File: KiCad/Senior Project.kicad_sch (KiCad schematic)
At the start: 26 parts, among them J1 USB_C_Receptacle_USB2.0_16P, J2 Screw_Terminal_01x02, J3 Screw_Terminal_01x06, SW1 SW_Push, SW2 SW_Push, U1 ESP32-S3FH4R2, X1 FC-135 32.7680KA-A5, Y2 Crystal_GND23

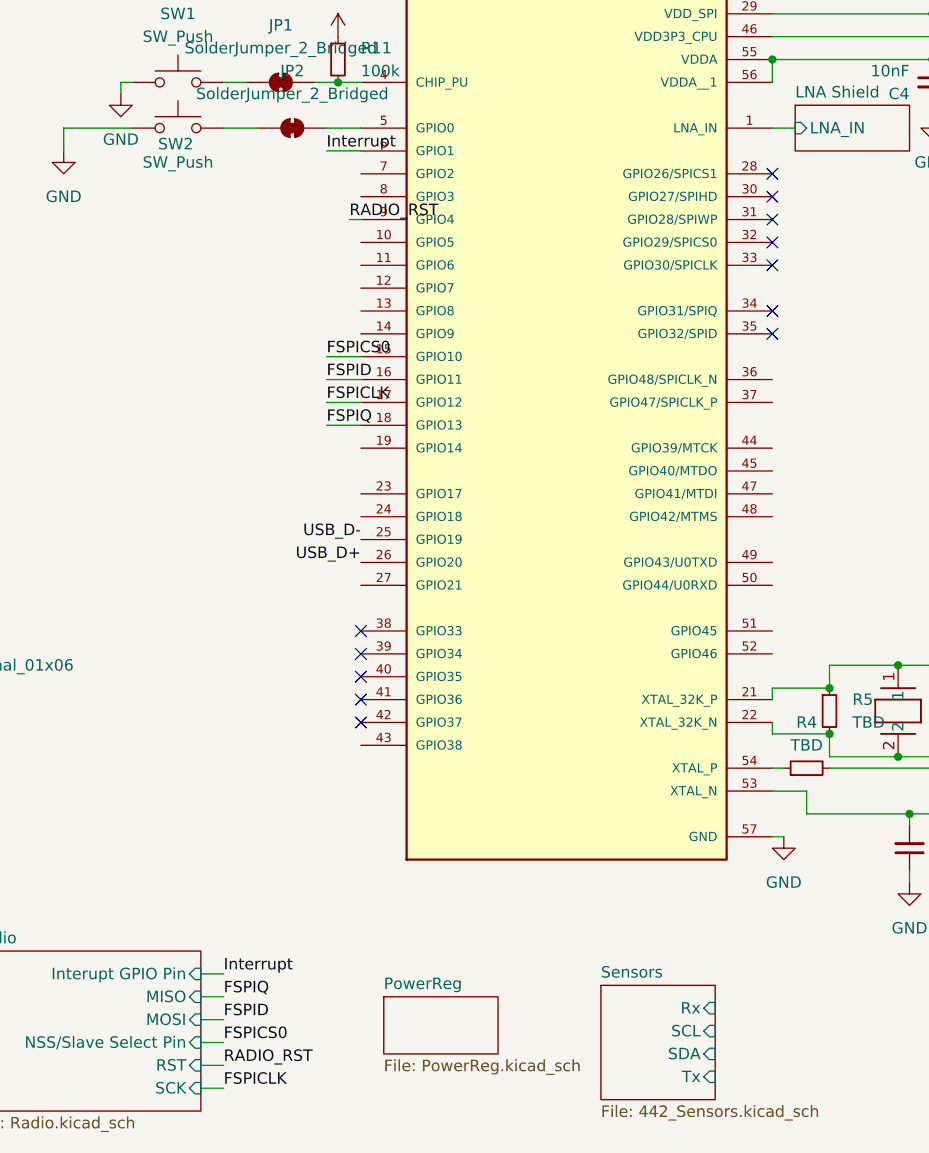
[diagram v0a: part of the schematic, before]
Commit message: I2C connections
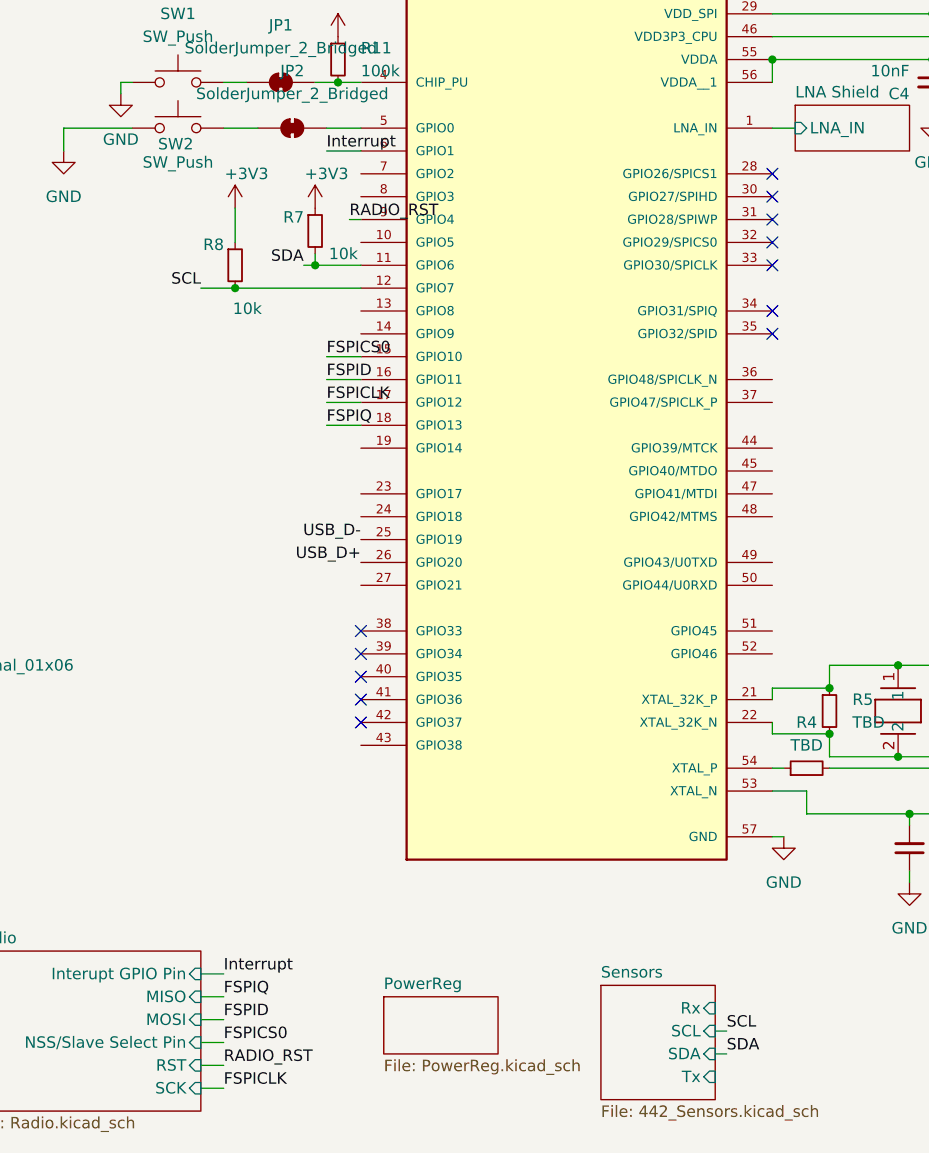
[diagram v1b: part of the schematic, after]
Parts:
- added R7, R8: 10k, Resistor_SMD:R_0402_1005Metric, symbol Device:R_Small
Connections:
- net +3V3: now also R7.1, R8.1
- net SDA: now reaches U1.11 (GPIO6)
- net SDA: now also R7.2
- net SCL: now reaches U1.12 (GPIO7)
- net SCL: now also R8.2

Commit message: Pin adjust
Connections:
- net SCL: now also U1.14 (GPIO9); no longer U1.12 (GPIO7)
- net SDA: now also U1.13 (GPIO8); no longer U1.11 (GPIO6)
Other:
- moved on the sheet: R7, R8
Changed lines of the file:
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@@
 	(paper "A4")
 	(junction
-		(at 106.68 85.09)
+		(at 118.11 62.23)
 		(diameter 0)
 		(color 0 0 0 0)
 	)
 	(junction
-		(at 118.11 62.23)
+		(at 181.61 143.51)
 		(diameter 0)
 		(color 0 0 0 0)
 	)
 	(junction
-		(at 181.61 143.51)
+		(at 105.41 90.17)
 		(diameter 0)
 		(color 0 0 0 0)
@@
 	)
 	(junction
+		(at 114.3 87.63)
+		(diameter 0)
+		(color 0 0 0 0)
+	)
+	(junction
 		(at 170.18 52.07)
 		(diameter 0)
@@
 		(color 0 0 0 0)
 	)
-	(junction
-		(at 115.57 82.55)
-		(diameter 0)
-		(color 0 0 0 0)
-	)
 	(no_connect
 		(at 166.37 74.93)
@@
 	(wire
 		(pts
-			(xy 102.87 85.09) (xy 106.68 85.09)
+			(xy 101.6 90.17) (xy 105.41 90.17)
 		)
 		(stroke
@@
 	(wire
 		(pts
-			(xy 114.3 82.55) (xy 115.57 82.55)
+			(xy 113.03 87.63) (xy 114.3 87.63)
+		)
+		(stroke
+			(width 0)
+			(type default)
+		)
+	)
+	(wire
+		(pts
+			(xy 105.41 90.17) (xy 120.65 90.17)
 		)
 		(stroke
@@
 	(wire
 		(pts
-			(xy 115.57 81.28) (xy 115.57 82.55)
+			(xy 114.3 86.36) (xy 114.3 87.63)
 		)
 		(stroke
@@
 	(wire
 		(pts
-			(xy 106.68 80.01) (xy 106.68 76.2)
+			(xy 105.41 85.09) (xy 105.41 81.28)
 		)
 		(stroke
@@
 	(wire
 		(pts
-			(xy 106.68 85.09) (xy 120.65 85.09)
-		)
-		(stroke
-			(width 0)
-			(type default)
-		)
-	)
-	(wire
-		(pts
 			(xy 64.77 49.53) (xy 69.85 49.53)
 		)
@@
 	(wire
 		(pts
-			(xy 115.57 82.55) (xy 120.65 82.55)
-		)
-		(stroke
-			(width 0)
-			(type default)
-		)
-	)
-	(wire
-		(pts
 			(xy 116.84 67.31) (xy 120.65 67.31)
 		)
@@
 	(wire
 		(pts
+			(xy 114.3 87.63) (xy 120.65 87.63)
+		)
+		(stroke
+			(width 0)
+			(type default)
+		)
+	)
+	(wire
+		(pts
 			(xy 102.87 163.83) (xy 105.41 163.83)
 		)
@@
 	)
 	(label "SDA"
-		(at 114.3 82.55 180)
+		(at 113.03 87.63 180)
 		(effects
 			(font
@@
 	)
 	(label "SCL"
-		(at 102.87 85.09 180)
+		(at 101.6 90.17 180)
 		(effects
 			(font
@@
 	(symbol
 		(lib_id "Device:R_Small")
-		(at 106.68 82.55 0)
+		(at 105.41 87.63 0)
 		(unit 1)
 		(exclude_from_sim no)
@@
 		(dnp no)
 		(property "Reference" "R8"
-			(at 103.124 80.264 0)
+			(at 101.854 85.344 0)
 			(effects
 				(font
@@
 		)
 		(property "Value" "10k"
-			(at 106.426 87.376 0)
+			(at 105.156 92.456 0)
 			(effects
 				(font
@@
 		)
 		(property "Footprint" "Resistor_SMD:R_0402_1005Metric"
-			(at 106.68 82.55 0)
+			(at 105.41 87.63 0)
 			(effects
 				(font
@@
 		)
 		(property "Datasheet" "~"
-			(at 106.68 82.55 0)
+			(at 105.41 87.63 0)
 			(effects
 				(font
@@
 		)
 		(property "Description" "Resistor, small symbol"
-			(at 106.68 82.55 0)
+			(at 105.41 87.63 0)
 			(effects
 				(font
@@
 	(symbol
 		(lib_id "power:+3V3")
-		(at 106.68 76.2 0)
+		(at 105.41 81.28 0)
 		(unit 1)
 		(exclude_from_sim no)
@@
 		(dnp no)
 		(property "Reference" "#PWR076"
-			(at 106.68 80.01 0)
+			(at 105.41 85.09 0)
 			(effects
 				(font
@@
 		)
 		(property "Value" "+3V3"
-			(at 107.95 72.39 0)
+			(at 106.68 77.47 0)
 			(effects
 				(font
@@
 		)
 		(property "Footprint" ""
-			(at 106.68 76.2 0)
+			(at 105.41 81.28 0)
 			(effects
 				(font
@@
 		)
 		(property "Datasheet" ""
-			(at 106.68 76.2 0)
+			(at 105.41 81.28 0)
 			(effects
 				(font
@@
 		)
 		(property "Description" "Power symbol creates a global label with name \"+3V3\""
-			(at 106.68 76.2 0)
+			(at 105.41 81.28 0)
 			(effects
 				(font
@@
 	(symbol
 		(lib_id "Device:R_Small")
-		(at 115.57 78.74 0)
+		(at 114.3 83.82 0)
 		(unit 1)
 		(exclude_from_sim no)
@@
 		(dnp no)
 		(property "Reference" "R7"
-			(at 112.014 77.216 0)
+			(at 110.744 82.296 0)
 			(effects
 				(font
@@
 		)
 		(property "Value" "10k"
-			(at 117.094 81.28 0)
+			(at 115.824 86.36 0)
 			(effects
 				(font
@@
 		)
 		(property "Footprint" "Resistor_SMD:R_0402_1005Metric"
-			(at 115.57 78.74 0)
+			(at 114.3 83.82 0)
 			(effects
 				(font
@@
 		)
 		(property "Datasheet" "~"
-			(at 115.57 78.74 0)
+			(at 114.3 83.82 0)
 			(effects
 				(font
@@
 		)
 		(property "Description" "Resistor, small symbol"
-			(at 115.57 78.74 0)
+			(at 114.3 83.82 0)
 			(effects
 				(font
@@
 	(symbol
 		(lib_id "power:+3V3")
-		(at 115.57 76.2 0)
+		(at 114.3 81.28 0)
 		(unit 1)
 		(exclude_from_sim no)
@@
 		(dnp no)
 		(property "Reference" "#PWR077"
-			(at 115.57 80.01 0)
+			(at 114.3 85.09 0)
 			(effects
 				(font
@@
 		)
 		(property "Value" "+3V3"
-			(at 116.84 72.39 0)
+			(at 115.57 77.47 0)
 			(effects
 				(font
@@
 		)
 		(property "Footprint" ""
-			(at 115.57 76.2 0)
+			(at 114.3 81.28 0)
 			(effects
 				(font
@@
 		)
 		(property "Datasheet" ""
-			(at 115.57 76.2 0)
+			(at 114.3 81.28 0)
 			(effects
 				(font
@@
 		)
 		(property "Description" "Power symbol creates a global label with name \"+3V3\""
-			(at 115.57 76.2 0)
+			(at 114.3 81.28 0)
 			(effects
 				(font

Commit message: Layout updated. Very little left to do.
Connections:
- net Sense 1: now reaches U1.19 (GPIO14)
- net Sense 2: now reaches U1.23 (GPIO17)
- net Sense 3: now reaches U1.24 (GPIO18)
- net Pyro GPIO 2: now reaches U1.36 (GPIO48/SPICLK_N)
- net Pyro GPIO 3: now reaches U1.37 (GPIO47/SPICLK_P)
- net Pyro GPIO 1: now reaches U1.43 (GPIO38)
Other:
- sheet Sensors ports: added GPS_Reset; removed none
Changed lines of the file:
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@@
 	(wire
 		(pts
+			(xy 41.91 137.16) (xy 43.18 137.16)
+		)
+		(stroke
+			(width 0)
+			(type default)
+		)
+	)
+	(wire
+		(pts
+			(xy 119.38 135.89) (xy 120.65 135.89)
+		)
+		(stroke
+			(width 0)
+			(type default)
+		)
+	)
+	(wire
+		(pts
+			(xy 166.37 97.79) (xy 167.64 97.79)
+		)
+		(stroke
+			(width 0)
+			(type default)
+		)
+	)
+	(wire
+		(pts
 			(xy 184.15 54.61) (xy 191.77 54.61)
 		)
@@
 	(wire
 		(pts
+			(xy 41.91 154.94) (xy 43.18 154.94)
+		)
+		(stroke
+			(width 0)
+			(type default)
+		)
+	)
+	(wire
+		(pts
 			(xy 102.87 161.29) (xy 105.41 161.29)
 		)
@@
 	(wire
 		(pts
+			(xy 41.91 139.7) (xy 43.18 139.7)
+		)
+		(stroke
+			(width 0)
+			(type default)
+		)
+	)
+	(wire
+		(pts
 			(xy 207.01 139.7) (xy 207.01 138.43)
 		)
@@
 	(wire
 		(pts
+			(xy 41.91 121.92) (xy 43.18 121.92)
+		)
+		(stroke
+			(width 0)
+			(type default)
+		)
+	)
+	(wire
+		(pts
 			(xy 116.84 95.25) (xy 120.65 95.25)
 		)
@@
 	(wire
 		(pts
+			(xy 41.91 124.46) (xy 43.18 124.46)
+		)
+		(stroke
+			(width 0)
+			(type default)
+		)
+	)
+	(wire
+		(pts
 			(xy 170.18 140.97) (xy 166.37 140.97)
 		)
@@
 	(wire
 		(pts
+			(xy 41.91 152.4) (xy 43.18 152.4)
+		)
+		(stroke
+			(width 0)
+			(type default)
+		)
+	)
+	(wire
+		(pts
 			(xy 170.18 52.07) (xy 172.72 52.07)
 		)
@@
 	(wire
 		(pts
+			(xy 166.37 95.25) (xy 167.64 95.25)
+		)
+		(stroke
+			(width 0)
+			(type default)
+		)
+	)
+	(wire
+		(pts
 			(xy 102.87 171.45) (xy 105.41 171.45)
 		)
@@
 		)
 	)
+	(label "Sense 2"
+		(at 43.18 139.7 0)
+		(effects
+			(font
+				(size 1.27 1.27)
+			)
+			(justify left bottom)
+		)
+	)
 	(label "SCL"
 		(at 161.29 167.64 0)
@@
 		)
 	)
+	(label "Sense 1"
+		(at 43.18 124.46 0)
+		(effects
+			(font
+				(size 1.27 1.27)
+			)
+			(justify left bottom)
+		)
+	)
 	(label "Interrupt"
 		(at 105.41 161.29 0)
@@
 		)
 	)
+	(label "Pyro GPIO 2"
+		(at 167.64 95.25 0)
+		(effects
+			(font
+				(size 1.27 1.27)
+			)
+			(justify left bottom)
+		)
+	)
 	(label "RADIO_RST"
 		(at 105.41 171.45 0)
@@
 		)
 	)
+	(label "Pyro GPIO 1"
+		(at 43.18 121.92 0)
+		(effects
+			(font
+				(size 1.27 1.27)
+			)
+			(justify left bottom)
+		)
+	)
+	(label "Pyro GPIO 1"
+		(at 119.38 135.89 180)
+		(effects
+			(font
+				(size 1.27 1.27)
+			)
+			(justify right bottom)
+		)
+	)
 	(label "FSPICLK"
 		(at 116.84 97.79 0)
@@
 		)
 	)
+	(label "Pyro GPIO 3"
+		(at 167.64 97.79 0)
+		(effects
+			(font
+				(size 1.27 1.27)
+			)
+			(justify left bottom)
+		)
+	)
 	(label "FSPICS0"
 		(at 116.84 92.71 0)
@@
 		)
 	)
+	(label "Sense 2"
+		(at 120.65 107.95 180)
+		(effects
+			(font
+				(size 1.27 1.27)
+			)
+			(justify right bottom)
+		)
+	)
 	(label "Interrupt"
 		(at 116.84 69.85 0)
@@
 		)
 	)
+	(label "Sense 1"
+		(at 120.65 102.87 180)
+		(effects
+			(font
+				(size 1.27 1.27)
+			)
+			(justify right bottom)
+		)
+	)
+	(label "Pyro GPIO 2"
+		(at 43.18 137.16 0)
+		(effects
+			(font
+				(size 1.27 1.27)
+			)
+			(justify left bottom)
+		)
+	)
 	(label "SDA"
 		(at 161.29 170.18 0)
@@
 		)
 	)
+	(label "Pyro GPIO 3"
+		(at 43.18 152.4 0)
+		(effects
+			(font
+				(size 1.27 1.27)
+			)
+			(justify left bottom)
+		)
+	)
+	(label "Sense 3"
+		(at 120.65 110.49 180)
+		(effects
+			(font
+				(size 1.27 1.27)
+			)
+			(justify right bottom)
+		)
+	)
 	(label "FSPID"
 		(at 116.84 95.25 0)
@@
 		)
 	)
+	(label "Sense 3"
+		(at 43.18 154.94 0)
+		(effects
+			(font
+				(size 1.27 1.27)
+			)
+			(justify left bottom)
+		)
+	)
 	(symbol
 		(lib_id "power:GND")
@@
 	(sheet
 		(at 147.32 162.56)
-		(size 12.7 12.7)
+		(size 12.7 15.24)
 		(exclude_from_sim no)
 		(in_bom yes)
@@
 		)
 		(property "Sheetfile" "442_Sensors.kicad_sch"
-			(at 147.32 175.8446 0)
+			(at 147.32 178.3846 0)
 			(effects
 				(font
@@
 			(effects
 				(font
+					(size 1.27 1.27)
+				)
+				(justify right)
+			)
+		)
+		(pin "GPS_Reset" input
+			(at 160.02 175.26 0)
+			(effects
+				(font

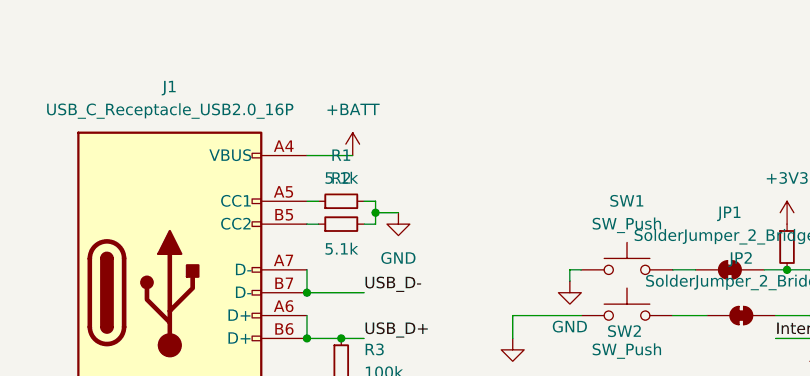
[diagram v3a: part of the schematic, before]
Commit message: Added a diode to prevent reverse current issues
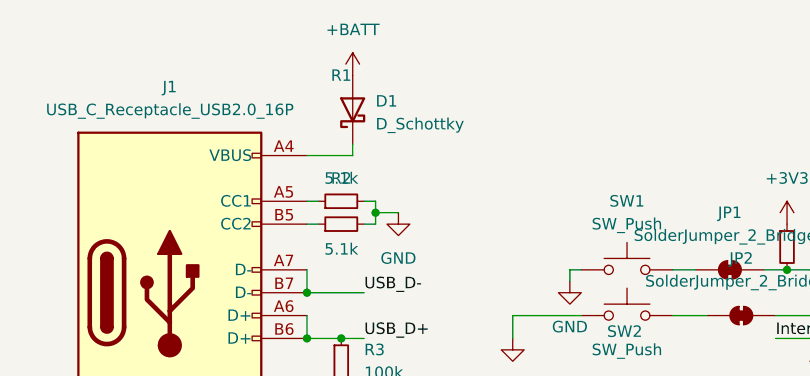
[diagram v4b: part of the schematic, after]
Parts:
- added D1: D_Schottky, symbol Device:D_Schottky
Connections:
- net +BATT: now also D1.2 (A); no longer J1.A4 (VBUS), J1.A9 (VBUS), J1.B4 (VBUS), J1.B9 (VBUS)
- new net: D1.1 (K), J1.A4 (VBUS), J1.A9 (VBUS), J1.B4 (VBUS), J1.B9 (VBUS)
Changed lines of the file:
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@@
 	(wire
 		(pts
+			(xy 69.85 48.26) (xy 69.85 49.53)
+		)
+		(stroke
+			(width 0)
+			(type default)
+		)
+	)
+	(wire
+		(pts
 			(xy 166.37 138.43) (xy 167.64 138.43)
 		)
@@
 	(wire
 		(pts
-			(xy 170.18 52.07) (xy 172.72 52.07)
+			(xy 64.77 49.53) (xy 69.85 49.53)
 		)
 		(stroke
@@
 	(wire
 		(pts
-			(xy 95.25 67.31) (xy 87.63 67.31)
+			(xy 170.18 52.07) (xy 172.72 52.07)
 		)
 		(stroke
@@
 	(wire
 		(pts
-			(xy 207.01 138.43) (xy 212.09 138.43)
+			(xy 95.25 67.31) (xy 87.63 67.31)
 		)
 		(stroke
@@
 	(wire
 		(pts
-			(xy 166.37 129.54) (xy 172.72 129.54)
+			(xy 207.01 138.43) (xy 212.09 138.43)
 		)
 		(stroke
@@
 	(wire
 		(pts
-			(xy 191.77 59.69) (xy 184.15 59.69)
+			(xy 166.37 129.54) (xy 172.72 129.54)
 		)
 		(stroke
@@
 	(wire
 		(pts
-			(xy 118.11 62.23) (xy 120.65 62.23)
+			(xy 191.77 59.69) (xy 184.15 59.69)
 		)
 		(stroke
@@
 	(wire
 		(pts
-			(xy 52.07 134.62) (xy 52.07 127)
+			(xy 118.11 62.23) (xy 120.65 62.23)
 		)
 		(stroke
@@
 	(wire
 		(pts
-			(xy 170.18 45.72) (xy 170.18 46.99)
+			(xy 52.07 134.62) (xy 52.07 127)
 		)
 		(stroke
@@
 	(wire
 		(pts
-			(xy 64.77 49.53) (xy 69.85 49.53)
+			(xy 170.18 45.72) (xy 170.18 46.99)
 		)
 		(stroke
@@
 	)
 	(symbol
+		(lib_id "Device:D_Schottky")
+		(at 69.85 44.45 90)
+		(unit 1)
+		(exclude_from_sim no)
+		(in_bom yes)
+		(on_board yes)
+		(dnp no)
+		(fields_autoplaced yes)
+		(property "Reference" "D1"
+			(at 72.39 43.4974 90)
+			(effects
+				(font
+					(size 1.27 1.27)
+				)
+				(justify right)
+			)
+		)
+		(property "Value" "D_Schottky"
+			(at 72.39 46.0374 90)
+			(effects
+				(font
+					(size 1.27 1.27)
+				)
+				(justify right)
+			)
+		)
+		(property "Footprint" ""
+			(at 69.85 44.45 0)
+			(effects
+				(font
+					(size 1.27 1.27)
+				)
+				(hide yes)
+			)
+		)
+		(property "Datasheet" "~"
+			(at 69.85 44.45 0)
+			(effects
+				(font
+					(size 1.27 1.27)
+				)
+				(hide yes)
+			)
+		)
+		(property "Description" "Schottky diode"
+			(at 69.85 44.45 0)
+			(effects
+				(font
+					(size 1.27 1.27)
+				)
+				(hide yes)
+			)
+		)
+		(pin "1"
+		)
+		(pin "2"
+		)
+		(instances
+			(project ""
+				(path "/16f8cce7-467e-4342-b55a-00af81cd6f69"
+					(reference "D1")
+					(unit 1)
+				)
+			)
+		)
+	)
+	(symbol
 		(lib_id "power:GND")
 		(at 41.91 88.9 0)
@@
 	(symbol
 		(lib_id "power:+BATT")
-		(at 69.85 49.53 0)
+		(at 69.85 40.64 0)
 		(unit 1)
 		(exclude_from_sim no)
@@
 		(fields_autoplaced yes)
 		(property "Reference" "#PWR04"
-			(at 69.85 53.34 0)
+			(at 69.85 44.45 0)
 			(effects
 				(font
@@
 		)
 		(property "Value" "+BATT"
-			(at 69.85 44.45 0)
+			(at 69.85 35.56 0)
 			(effects
 				(font
@@
 		)
 		(property "Footprint" ""
-			(at 69.85 49.53 0)
+			(at 69.85 40.64 0)
 			(effects
 				(font
@@
 		)
 		(property "Datasheet" ""
-			(at 69.85 49.53 0)
+			(at 69.85 40.64 0)
 			(effects
 				(font
@@
 		)
 		(property "Description" "Power symbol creates a global label with name \"+BATT\""
-			(at 69.85 49.53 0)
+			(at 69.85 40.64 0)
 			(effects
 				(font
@@
 			)
 		)
-		(property "Datasheet" "https://www.usb.org/sites/default/files/documents/usb_type-c.zip"
+		(property "Datasheet" "https://jlcpcb.com/api/file/downloadByFileSystemAccessId/8589784508607737856"
 			(at 53.34 64.77 0)
 			(effects
@@
 		(on_board yes)
 		(dnp no)
-		(fields_autoplaced yes)
 		(property "Reference" "R1"
-			(at 68.58 49.53 90)
+			(at 68.58 40.64 90)
 			(effects
 				(font
